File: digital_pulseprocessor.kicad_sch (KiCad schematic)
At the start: 17 parts, among them J300 SolderJumper_2_Open, J310 Conn_02x03_Odd_Even, U300 SN74LV221AD, U301 SN74LV221AD

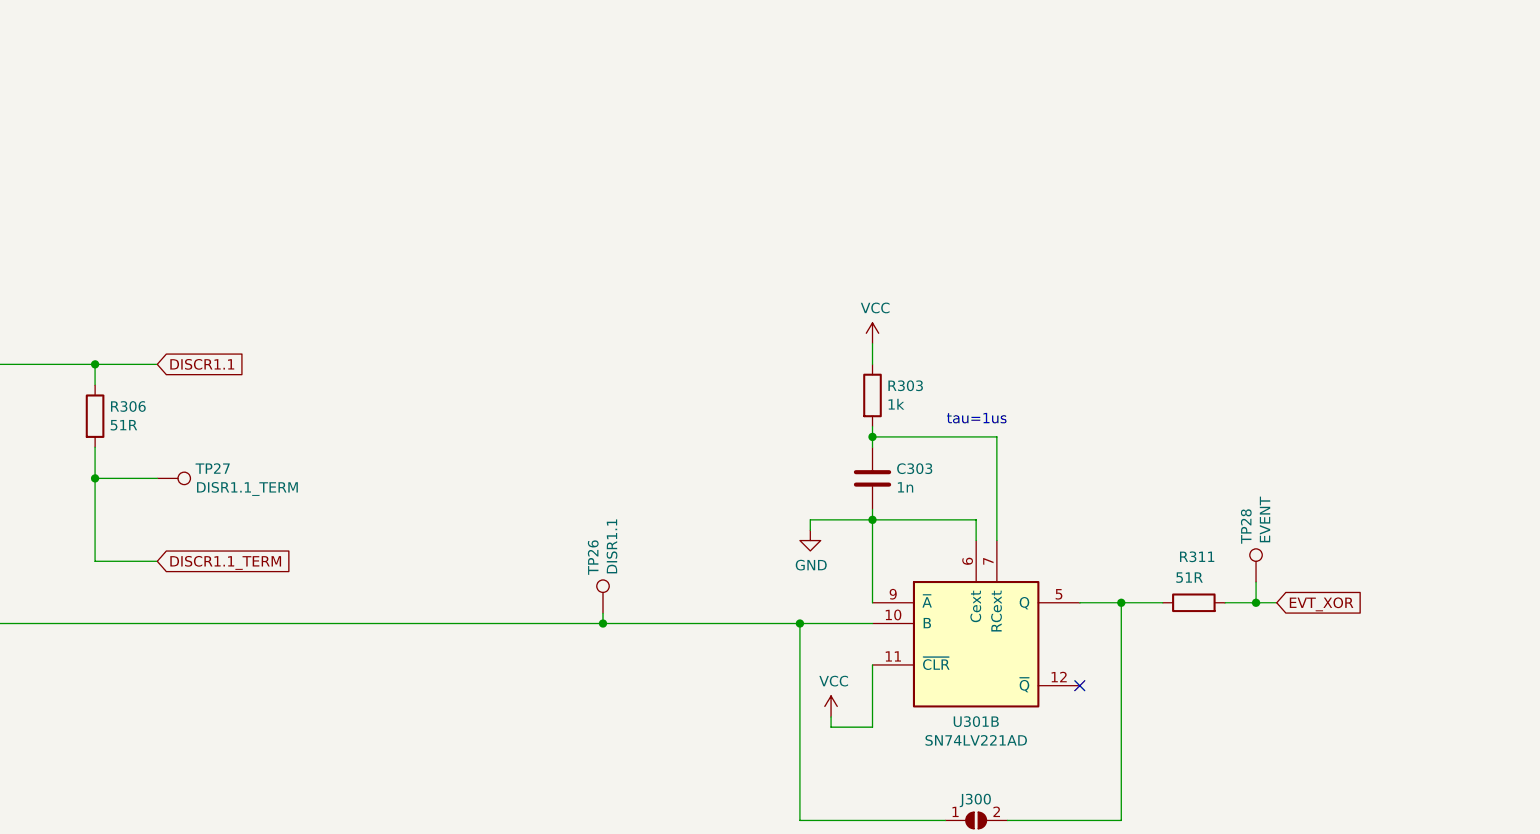
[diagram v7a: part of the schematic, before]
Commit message: Notes added in Schematics. Vias added on PCB.
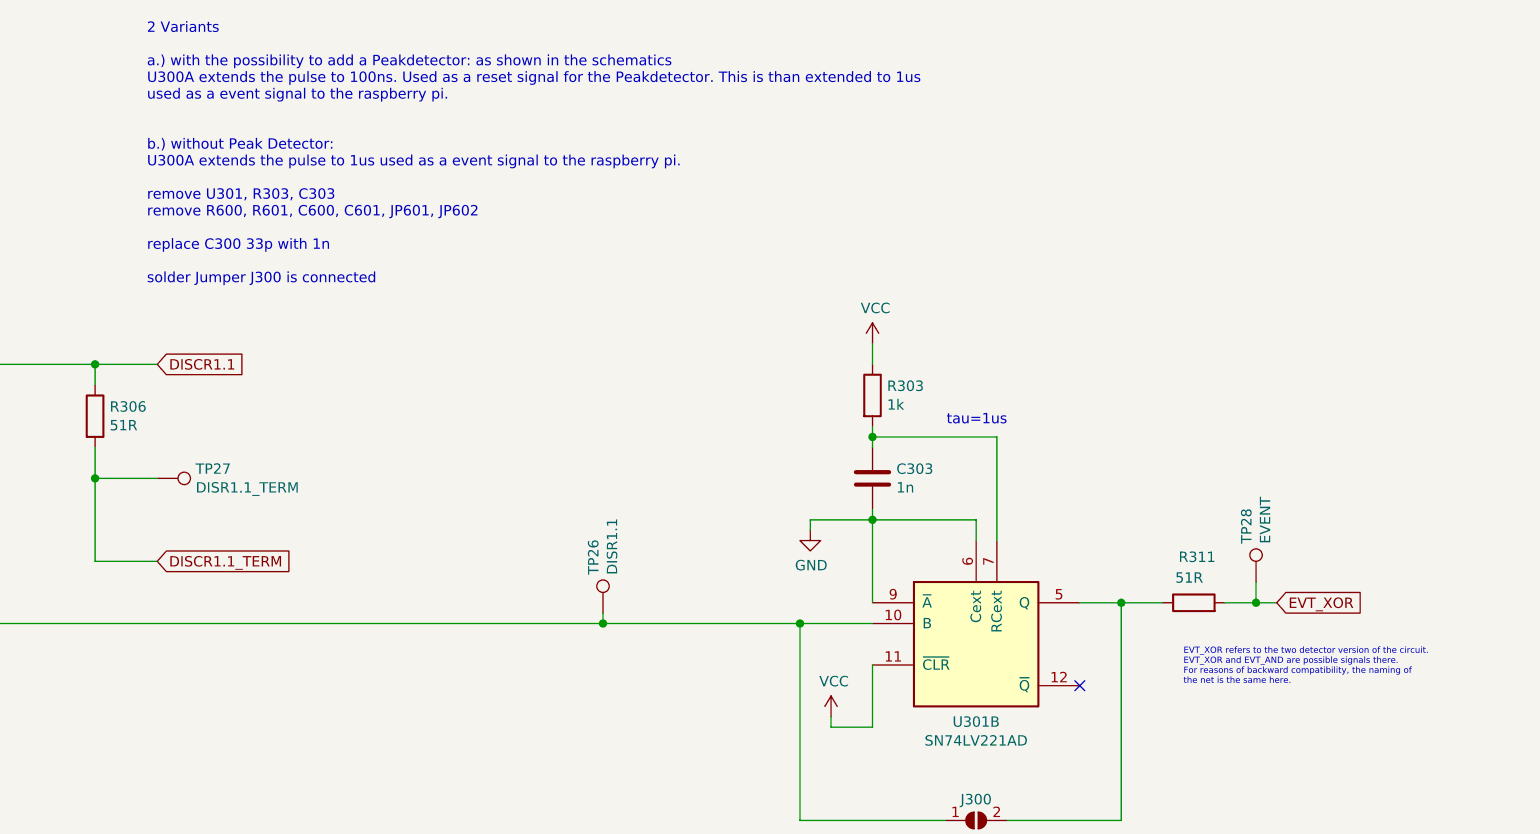
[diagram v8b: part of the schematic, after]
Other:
- note added: "2 Variants a.) with the possibility to add a Peakdetector: as shown in the schematics U300A extends the pulse to 100ns. Used as a reset signal for the Peakdetector. This is than extended to 1us used as a event signal to the raspberry pi. b.) without Peak Detector: U300A extends the pulse to 1us used as a event signal to the raspberry pi. remove U301, R303, C303 remove R600, R601, C600, C601, JP60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"
- note added: "EVT_XOR refers to the two detector version of the circuit. EVT_XOR and EVT_AND are possible signals there. For reasons of backward compatibility, the naming of the net is the same here."
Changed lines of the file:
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@@
     (effects (font (size 1.27 1.27)) (justify right bottom))
+  )
+  (text "2 Variants\n\na.) with the possibility to add a Peakdetector: as shown in the schematics\nU300A extends the pulse to 100ns. Used as a reset signal for the Peakdetector. This is than extended to 1us\nused as a event signal to the raspberry pi.\n\n\nb.) without Peak Detector:\nU300A extends the pulse to 1us used as a event signal to the raspberry pi. \n \nremove U301, R303, C303\nremove R600, R601, C600, C601, JP601, JP602\n\nreplace C300 33p with 1n\n\nsolder Jumper J300 is connected\n\n"
+    (at 120.65 49.53 0)
+    (effects (font (size 1.27 1.27)) (justify left bottom))
   )
   (text "tau=1us" (at 226.06 64.77 180)
     (effects (font (size 1.27 1.27)) (justify right bottom))
   )
+  (text "EVT_XOR refers to the two detector version of the circuit. \nEVT_XOR and EVT_AND are possible signals there. \nFor reasons of backward compatibility, the naming of\nthe net is the same here."
+    (at 247.65 96.52 0)
+    (effects (font (size 0.762 0.762)) (justify left bottom))
+  )
   (global_label "COMP1" (shape input) (at 54.61 59.69 180)
